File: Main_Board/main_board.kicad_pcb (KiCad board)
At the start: 2 copper layers, 158.5 x 152.1 mm, 15 parts, among them J1 MEGA_SARJ, J2 POWER, J3 I2C, J4 FREE_GPIO, J5 5V, J6 12V, J7 24V, J8 GND, J9 GND, U1 BNO055_IMU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

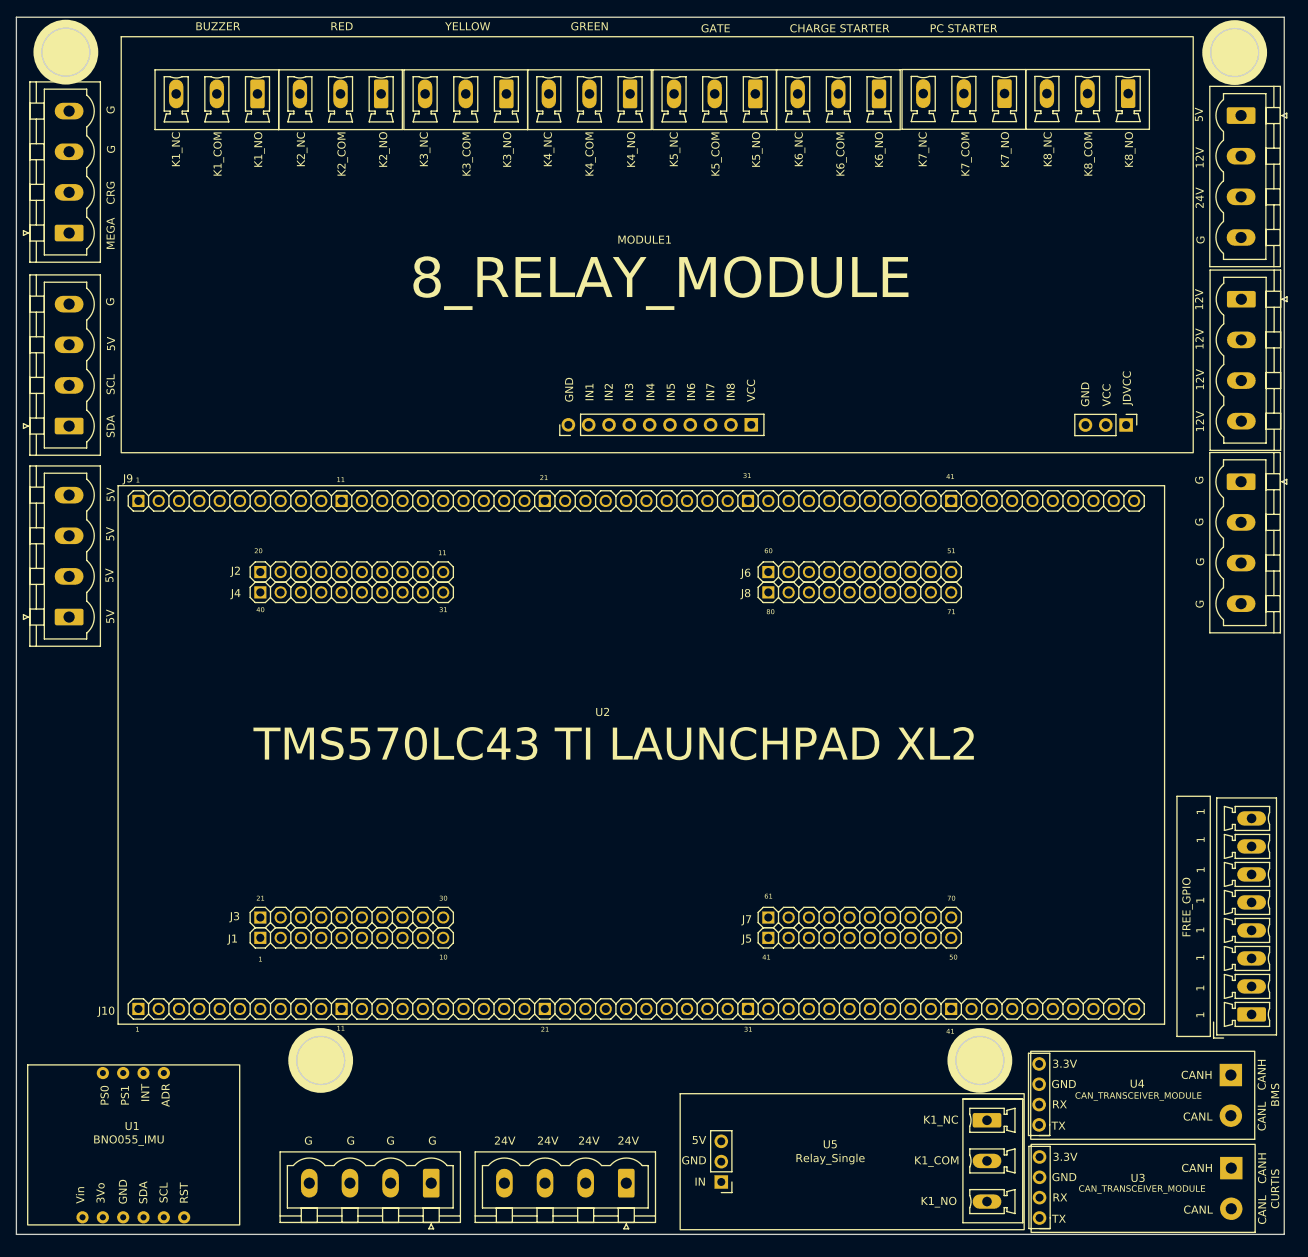
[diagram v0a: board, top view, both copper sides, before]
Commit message: all pcb design except routing completed.
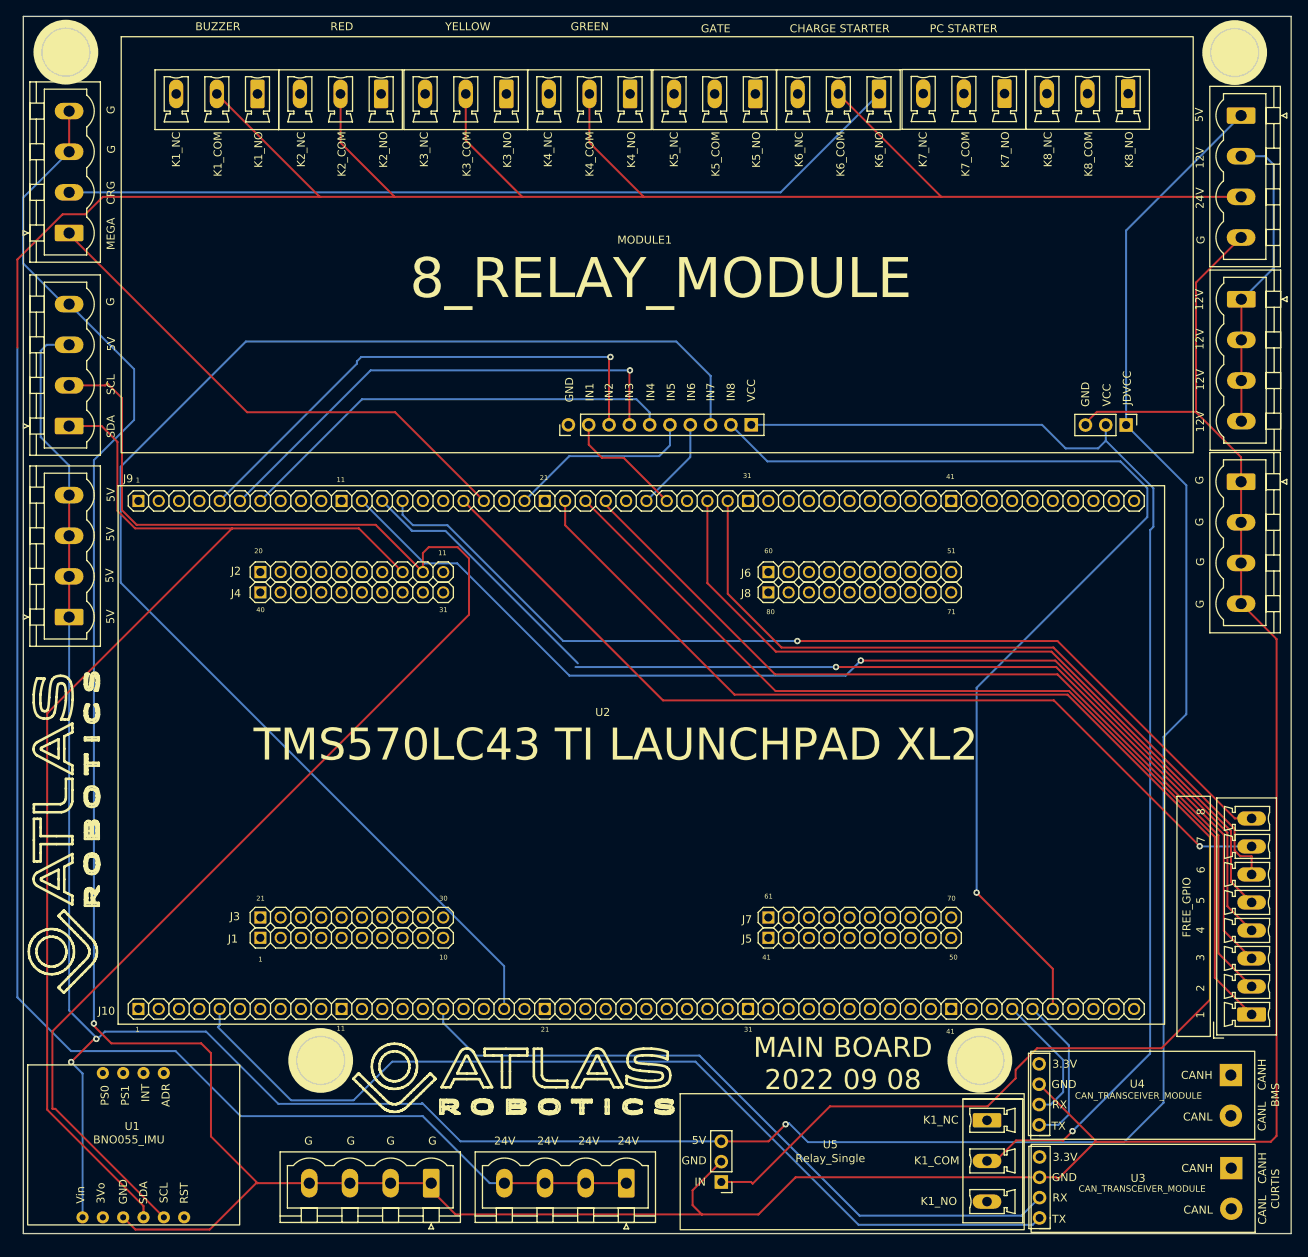
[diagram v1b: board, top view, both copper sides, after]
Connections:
- J4 pad 1: unconnected-(J4-Pad1) -> N2HET2_23
- J4 pad 2: unconnected-(J4-Pad2) -> N2HET2_11
- J4 pad 3: unconnected-(J4-Pad3) -> DCAN2TX
- J4 pad 4: unconnected-(J4-Pad4) -> DCAN2RX
- J4 pad 5: unconnected-(J4-Pad5) -> AD2IN_23
- J4 pad 6: unconnected-(J4-Pad6) -> AD2IN_24
- J4 pad 7: unconnected-(J4-Pad7) -> N2HET2_3/MIBSPI2CLK
- J4 pad 8: unconnected-(J4-Pad8) -> N2HET2_4
- MODULE1 pad 5: N2HET2_0 -> N2HET2_9
- MODULE1 pad 6: N2HET2_1/N2HET1_NDIS -> N2HET2_0
- MODULE1 pad 7: N2HET2_6 -> N2HET2_1/N2HET1_NDIS
- MODULE1 pad 8: N2HET2_7/MIBSPI2NCS_0 -> N2HET2_6
- MODULE1 pad 9: N2HET2_9 -> N2HET2_7/MIBSPI2NCS_0
- U2 pad J10_3: unconnected-(U2-PadJ10_3) -> +3V3
- U2 pad J10_46: unconnected-(U2-PadJ10_46) -> N2HET2_13/MIBSPI2SOMI
- U2 pad J9_29: unconnected-(U2-PadJ9_29) -> AD2IN_23
- U2 pad J9_3: unconnected-(U2-PadJ9_3) -> +3V3
- U2 pad J9_30: unconnected-(U2-PadJ9_30) -> AD2IN_24
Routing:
- net GND: track 0.00 -> 465.4 mm, vias 0 -> 1
- net +24V: track 0.00 -> 419.2 mm
- net +5V: track 0.00 -> 394.2 mm, vias 0 -> 3
- net N2HET2_14/MIBSPI2SIMO: track 0.00 -> 191.4 mm
- net MIBSPI3NCS_3/I2C1_SCL/N2HET1_29/NTZ1_1: track 0.00 -> 181.2 mm
- net N2HET2_8: track 0.00 -> 175.8 mm
- net MIBSPI3NCS_2/I2C1_SDA/N2HET1_27/NTZ1_2: track 0.00 -> 155.0 mm
- net +3.3V: track 0.00 -> 153.1 mm, vias 0 -> 1
- net DCAN2RX: track 0.00 -> 140.4 mm, vias 0 -> 1
- net DCAN2TX: track 0.00 -> 139.5 mm, vias 0 -> 1
- net N2HET2_13/MIBSPI2SOMI: track 0.00 -> 133.2 mm, vias 0 -> 1
- net N2HET2_4: track 0.00 -> 123.7 mm, vias 0 -> 1
- net N2HET2_23: track 0.00 -> 120.2 mm
- net GIOB_2/DCAN4TX: track 0.00 -> 119.7 mm
- net N2HET2_3/MIBSPI2CLK: track 0.00 -> 116.4 mm, vias 0 -> 1
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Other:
- outline, holes or cut-outs redrawn
- board text added: "2"
- board text added: "3"
- board text added: "4"
- board text added: "5"
- board text added: "6"
- board text added: "7"
- board text added: "8"
- board text added: "MAIN BOARD 2022 09 08"

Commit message: pcb to completed gerber completed ready to print the PCB
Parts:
- moved J8 0.56 mm to (167.8, 75.2)
- moved J2 0.46 mm to (167.8, 28.4)
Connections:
- MODULE1 pad 13: +3.3V -> +3V3
- MODULE1 pad 2: +3.3V -> +3V3
- U2 pad J10_3: +3V3 -> unconnected-(U2-PadJ10_3)
- U5 pad 2: +3.3V -> +3V3
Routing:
- net +3V3: track 0.00 -> 232.5 mm
- net +3.3V: track 153.1 -> 0.00 mm, vias 1 -> 0
- net GND: track 465.4 -> 533.5 mm
- net MIBSPI3NCS_3/I2C1_SCL/N2HET1_29/NTZ1_1: track 181.2 -> 155.5 mm, vias 0 -> 2
- net /TRANSCEIVER_ON_OFF: track 0.00 -> 22.3 mm
- net N2HET2_8: track 175.8 -> 196.0 mm
- net N2HET2_0: track 65.0 -> 52.6 mm, vias 1 -> 0
- net N2HET2_1/N2HET1_NDIS: track 62.3 -> 52.6 mm, vias 1 -> 0
- net MIBSPI3NCS_2/I2C1_SDA/N2HET1_27/NTZ1_2: track 155.0 -> 147.2 mm
- net N2HET2_13/MIBSPI2SOMI: track 133.2 -> 126.7 mm, vias 1 -> 0
- net +5V: track 394.2 -> 400.3 mm, vias 3 -> 2
- net GIOB_2/DCAN4TX: track 119.7 -> 113.8 mm
- net +24V: track 419.2 -> 423.6 mm
- net N2HET2_6: track 56.2 -> 52.6 mm
- net N2HET2_14/MIBSPI2SIMO: track 191.4 -> 188.9 mm
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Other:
- board size 158.5 x 152.1 mm -> 158.5 x 153 mm
